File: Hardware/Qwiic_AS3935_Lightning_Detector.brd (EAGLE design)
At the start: 25.4 x 25.4 mm, 57 parts, among them U1 AS3935

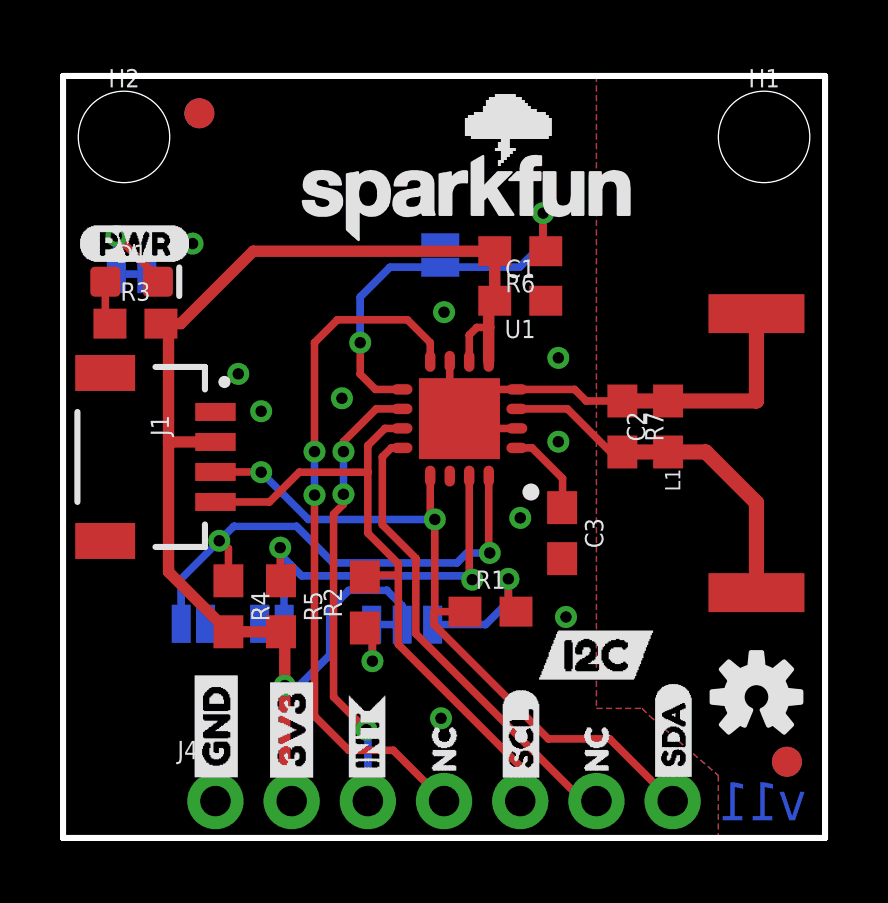
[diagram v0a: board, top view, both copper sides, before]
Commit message: Adds flame to underside (hur hur), adds additional path in bottom pour. changes jumper names to address rather than jumper
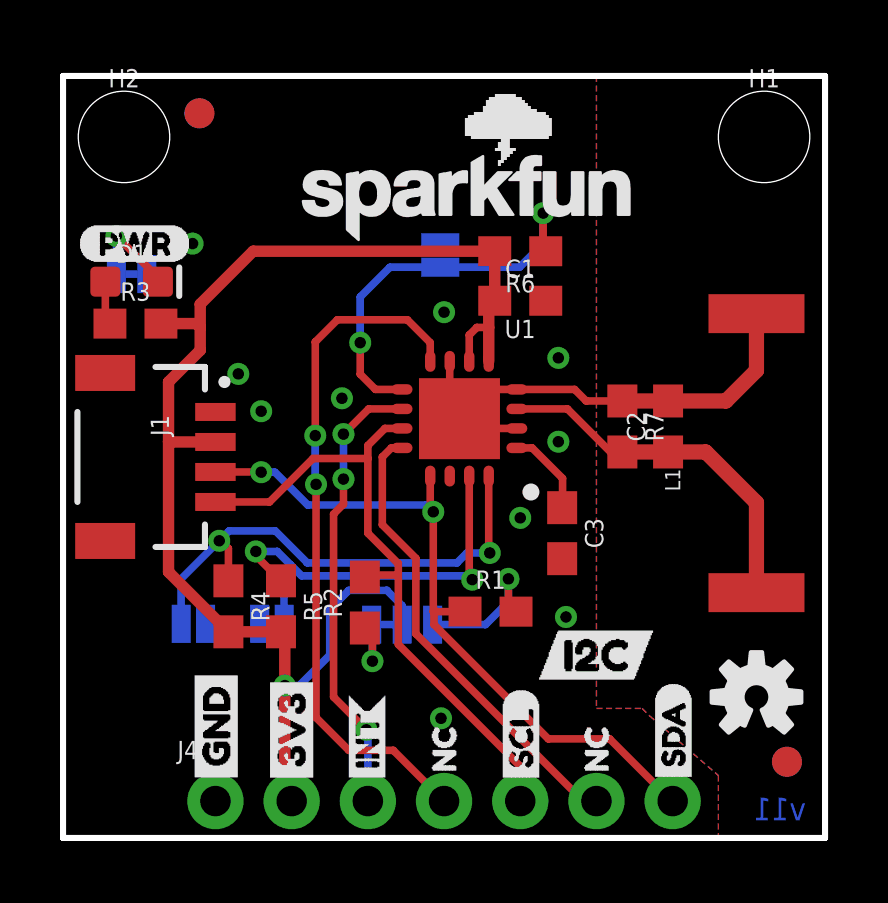
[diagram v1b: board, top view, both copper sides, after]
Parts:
- removed U$31: (no value), SparkFun-Aesthetics:OSHW-LOGO-S
- added LOGO3: SFE_LOGO_FLAME.2_INCH, SparkFun-Aesthetics:SFE_LOGO_FLAME_.2
- renumbered JP1 to ADD1, JP2 to ADD0
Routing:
- net 3.3V: track 44.7 -> 45.6 mm
- net GND: track 14.9 -> 14.3 mm
- net ADD0: track 14.1 -> 14.7 mm

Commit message: Fixes LED label
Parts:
- moved U$1 0.75 mm to (4.71, 16.7)
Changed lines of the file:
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@@
 <layer number="19" name="Unrouted" color="6" fill="1" visible="yes" active="yes"/>
 <layer number="20" name="Dimension" color="15" fill="1" visible="yes" active="yes"/>
-<layer number="21" name="tPlace" color="16" fill="1" visible="yes" active="yes"/>
+<layer number="21" name="tPlace" color="16" fill="1" visible="no" active="yes"/>
 <layer number="22" name="bPlace" color="14" fill="1" visible="yes" active="yes"/>
 <layer number="23" name="tOrigins" color="15" fill="1" visible="yes" active="yes"/>
@@
 <attribute name="VALUE" x="2.286" y="17.653" size="0.6096" layer="28" font="vector" ratio="20" rot="MR0" align="top-center"/>
 </element>
-<element name="U$1" library="LED" package="LED0" value="" x="4.003040625" y="16.957040625" smashed="yes" rot="MR0"/>
+<element name="U$1" library="LED" package="LED0" value="" x="4.714240625" y="16.728440625" smashed="yes" rot="MR0"/>
 <element name="U$2" library="DataLines" package="I2C0" value="" x="15.748" y="6.096" smashed="yes"/>
 <element name="U$3" library="DataLines" package="SPI1" value="" x="19.812" y="7.112" smashed="yes" rot="MR0"/>

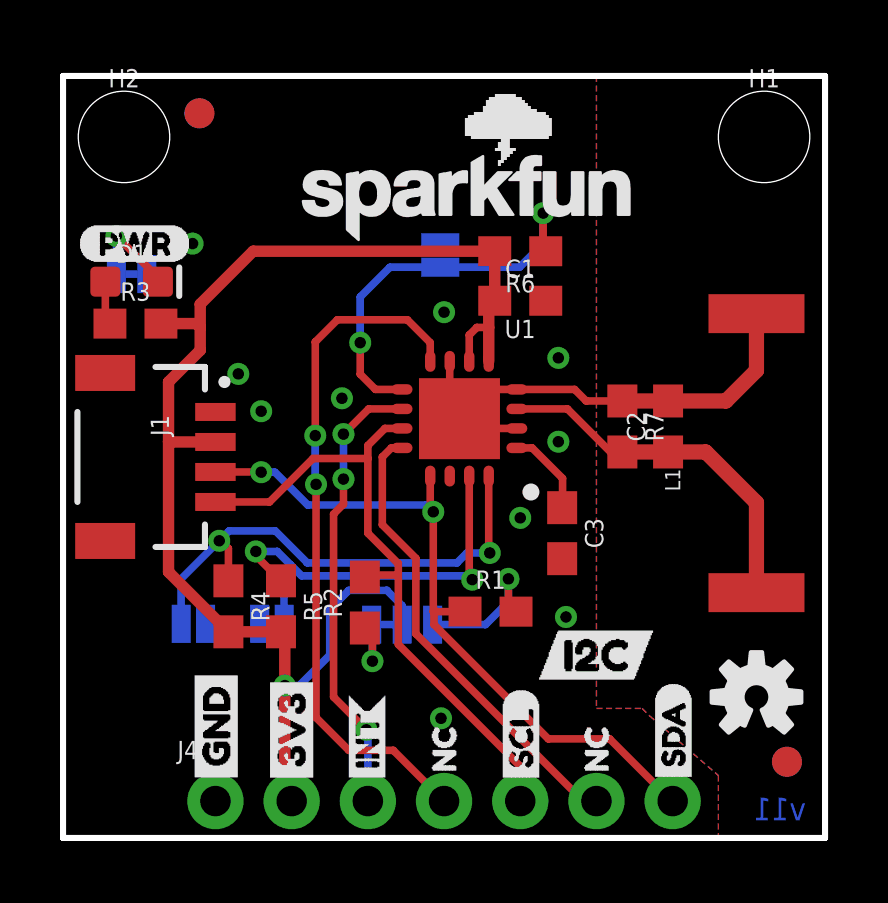
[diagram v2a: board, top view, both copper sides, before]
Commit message: Removes old production files, updates board to default to SPI....
* Changes three way jumper to normally open - only need pull ups for I2C mode
* Changes interface select jumper to normally closed (SPI selection)
* Updates notes on both jumpers for these modes
* Removes Qwiic Header
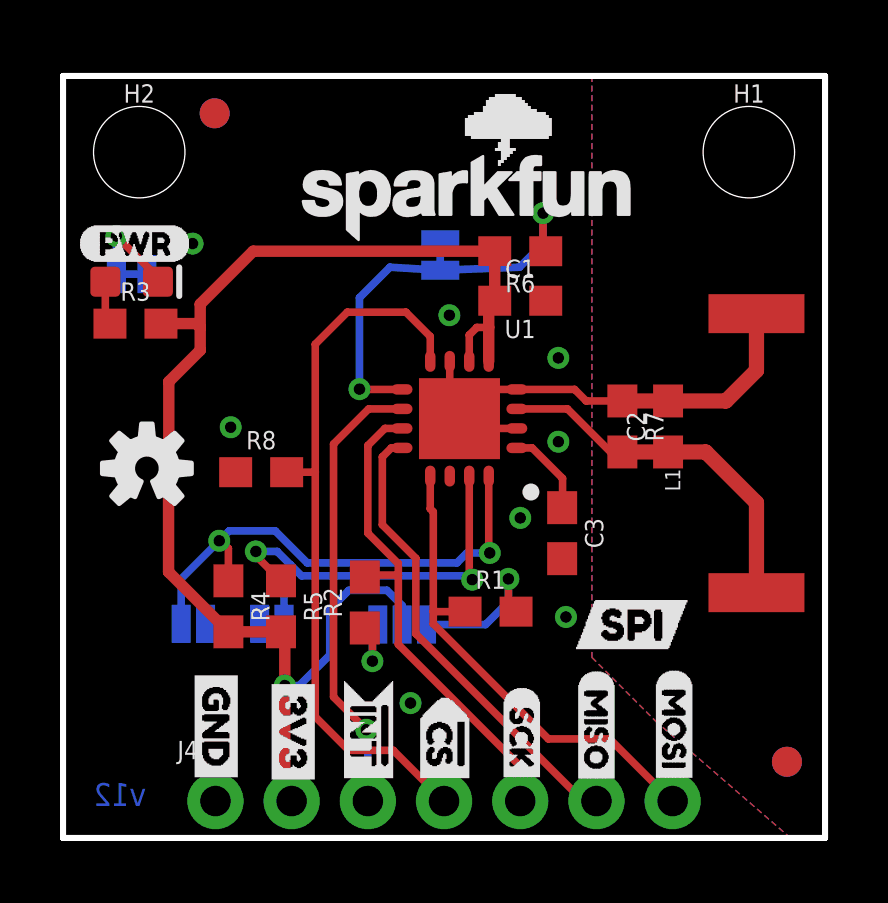
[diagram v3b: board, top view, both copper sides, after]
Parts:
- removed J1: (no value), SparkFun-Connectors:JST04_1MM_RA
- removed U$21: (no value), Labels:3V3-03
- removed U$24: (no value), INT_2:INT0
- removed U$25: (no value), SDA:SDA0
- removed U$28: (no value), SCL:SCL0
- added R8: 10k, SparkFun-Resistors:0603
- added U$11: (no value), Labels:MOSI-(]-03
- added U$13: (no value), INT:#INT0
- added U$15: (no value), DataLines:SPI1
- added U$9: (no value), Labels:MISO-(]-03
- JP3: value JUMPER-SMT_2_NO_SILK -> JUMPER-SMT_2_NC_TRACE_SILK; device SparkFun-Jumpers:SMT-JUMPER_2_NO_SILK -> SparkFun-Jumpers:SMT-JUMPER_2_NC_TRACE_SILK
- JP4: value JUMPER-SMT_3_1-NC_TRACE_SILK -> JUMPER-SMT_3_NO_SILK; device SparkFun-Jumpers:SMT-JUMPER_3_1-NC_TRACE_SILK -> SparkFun-Jumpers:SMT-JUMPER_3_NO_SILK
- U$14: device INT:INT0 -> INT:#INT0
- U$2: device DataLines:I2C0 -> Labels:GND-03
- U$4: device DataLines:NC2 -> Labels:3V3-03
- U$5: device DataLines:NC2 -> CS_2:#CS0
- U$8: device Labels:GND-03 -> Labels:SCK-(]-03
- moved LOGO1 21.7 mm to (2.79, 12.3)
- moved U$8 10.8 mm to (15.3, 5.05), flipped to the bottom, turned to 270 degrees
- moved U$2 10.6 mm to (5.11, 5.84), flipped to the bottom, turned to 270 degrees
- moved U$4 6.47 mm to (7.67, 5.59), flipped to the bottom, turned to 270 degrees
- moved U$5 6.11 mm to (12.7, 4.95), flipped to the bottom, turned to 270 degrees
- moved U$3 2.79 mm to (17.0, 7.11), flipped to the top
- moved H2 0.72 mm to (2.54, 22.9)
- moved H1 0.72 mm to (22.9, 22.9)
- moved U$14 0.69 mm to (10.2, 5.51)
- moved FD1 0.51 mm to (5.05, 24.2)
- moved FD4 0.51 mm to (5.05, 24.2)
- moved U$18 0.14 mm to (7.67, 5.59), flipped to the top
- moved U$30 0.13 mm to (12.7, 4.95), flipped to the top
- moved U$10 0.13 mm to (5.11, 5.84), flipped to the top
- moved U$23 0.11 mm to (15.3, 5.05), flipped to the top
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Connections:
- net !CS: now also R8.2
- net 3.3V: no longer J1.2
- net GND: now also R8.1; no longer J1.1
- net MOSI/SDA: no longer J1.3
- net SCLK/SCL: no longer J1.4
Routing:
- net MOSI/SDA: track 24.3 -> 16.5 mm, vias 2 -> 0
- net SCLK/SCL: track 22.2 -> 16.5 mm
- net 3.3V: track 45.6 -> 44.0 mm
- net !CS: track 23.0 -> 24.3 mm, vias 2 -> 0
- net INT: vias 3 -> 1
- net GND: vias 10 -> 8
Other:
- board text added: "v12"
- board text removed: "v11"
